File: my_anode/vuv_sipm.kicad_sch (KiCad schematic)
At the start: 8 parts

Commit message: Add files via upload
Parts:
- renumbered C1 to C23, C2 to C24, D1 to D12, R1 to R56, R2 to R57, R3 to R58, R4 to R59, R5 to R60
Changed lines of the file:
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@@
   (symbol (lib_id "Device:R_US") (at 139.7 77.47 270) (unit 1)
     (in_bom yes) (on_board yes) (fields_autoplaced)
-    (property "Reference" "R4" (id 0) (at 140.9701 80.01 0)
+    (property "Reference" "R59" (id 0) (at 140.9701 80.01 0)
       (effects (font (size 1.27 1.27)) (justify left))
     )
@@
   (symbol (lib_id "Device:C") (at 115.57 73.66 90) (unit 1)
     (in_bom yes) (on_board yes) (fields_autoplaced)
-    (property "Reference" "C1" (id 0) (at 115.57 66.04 90))
+    (property "Reference" "C23" (id 0) (at 115.57 66.04 90))
     (property "Value" "C" (id 1) (at 115.57 68.58 90))
     (property "Footprint" "Capacitor_SMD:CP_Elec_4x3" (id 2) (at 119.38 72.6948 0)
@@
   (symbol (lib_id "Device:D_Photo") (at 124.46 91.44 180) (unit 1)
     (in_bom yes) (on_board yes) (fields_autoplaced)
-    (property "Reference" "D1" (id 0) (at 125.4125 85.09 0))
+    (property "Reference" "D12" (id 0) (at 125.4125 85.09 0))
     (property "Value" "D_Photo" (id 1) (at 125.4125 87.63 0))
     (property "Footprint" "OptoDevice:S13370-6075CN" (id 2) (at 125.73 91.44 0)
@@
   (symbol (lib_id "Device:R_US") (at 104.14 77.47 0) (unit 1)
     (in_bom yes) (on_board yes) (fields_autoplaced)
-    (property "Reference" "R1" (id 0) (at 106.68 76.1999 0)
+    (property "Reference" "R56" (id 0) (at 106.68 76.1999 0)
       (effects (font (size 1.27 1.27)) (justify left))
     )
@@
   (symbol (lib_id "Device:R_US") (at 113.03 88.9 0) (unit 1)
     (in_bom yes) (on_board yes) (fields_autoplaced)
-    (property "Reference" "R2" (id 0) (at 115.57 87.6299 0)
+    (property "Reference" "R57" (id 0) (at 115.57 87.6299 0)
       (effects (font (size 1.27 1.27)) (justify left))
     )
@@
   (symbol (lib_id "Device:R_US") (at 148.59 73.66 0) (unit 1)
     (in_bom yes) (on_board yes) (fields_autoplaced)
-    (property "Reference" "R5" (id 0) (at 151.13 72.3899 0)
+    (property "Reference" "R60" (id 0) (at 151.13 72.3899 0)
       (effects (font (size 1.27 1.27)) (justify left))
     )
@@
   (symbol (lib_id "Device:C") (at 140.97 93.98 0) (unit 1)
     (in_bom yes) (on_board yes) (fields_autoplaced)
-    (property "Reference" "C2" (id 0) (at 144.78 92.7099 0)
+    (property "Reference" "C24" (id 0) (at 144.78 92.7099 0)
       (effects (font (size 1.27 1.27)) (justify left))
     )
@@
   (symbol (lib_id "Device:R_US") (at 134.62 97.79 90) (unit 1)
     (in_bom yes) (on_board yes) (fields_autoplaced)
-    (property "Reference" "R3" (id 0) (at 133.3499 95.25 0)
+    (property "Reference" "R58" (id 0) (at 133.3499 95.25 0)
       (effects (font (size 1.27 1.27)) (justify left))
     )

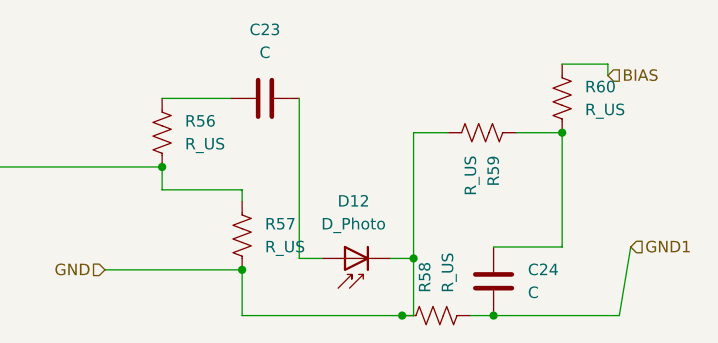
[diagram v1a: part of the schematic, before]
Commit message: Add quarter-anode board
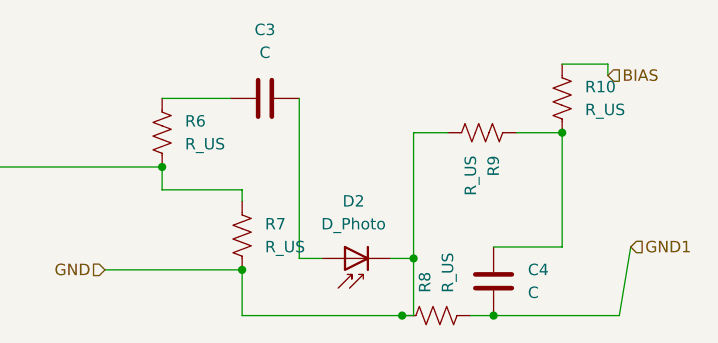
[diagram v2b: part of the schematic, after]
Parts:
- C3: renamed from C23; footprint Capacitor_SMD:CP_Elec_4x3 -> Capacitor_SMD:C_1812_4532Metric_Pad1.57x3.40mm_HandSolder
- C4: renamed from C24; footprint Capacitor_SMD:CP_Elec_4x3 -> Capacitor_SMD:C_1812_4532Metric_Pad1.57x3.40mm_HandSolder
- renumbered D12 to D2, R60 to R10, R56 to R6, R57 to R7, R58 to R8, R59 to R9
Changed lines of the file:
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@@
   (symbol (lib_id "Device:R_US") (at 139.7 77.47 270) (unit 1)
     (in_bom yes) (on_board yes) (fields_autoplaced)
-    (property "Reference" "R59" (id 0) (at 140.9701 80.01 0)
+    (property "Reference" "R9" (id 0) (at 140.9701 80.01 0)
       (effects (font (size 1.27 1.27)) (justify left))
     )
@@
   (symbol (lib_id "Device:C") (at 115.57 73.66 90) (unit 1)
     (in_bom yes) (on_board yes) (fields_autoplaced)
-    (property "Reference" "C23" (id 0) (at 115.57 66.04 90))
+    (property "Reference" "C3" (id 0) (at 115.57 66.04 90))
     (property "Value" "C" (id 1) (at 115.57 68.58 90))
-    (property "Footprint" "Capacitor_SMD:CP_Elec_4x3" (id 2) (at 119.38 72.6948 0)
+    (property "Footprint" "Capacitor_SMD:C_1812_4532Metric_Pad1.57x3.40mm_HandSolder" (id 2) (at 119.38 72.6948 0)
       (effects (font (size 1.27 1.27)) hide)
     )
@@
   (symbol (lib_id "Device:D_Photo") (at 124.46 91.44 180) (unit 1)
     (in_bom yes) (on_board yes) (fields_autoplaced)
-    (property "Reference" "D12" (id 0) (at 125.4125 85.09 0))
+    (property "Reference" "D2" (id 0) (at 125.4125 85.09 0))
     (property "Value" "D_Photo" (id 1) (at 125.4125 87.63 0))
     (property "Footprint" "OptoDevice:S13370-6075CN" (id 2) (at 125.73 91.44 0)
@@
   (symbol (lib_id "Device:R_US") (at 104.14 77.47 0) (unit 1)
     (in_bom yes) (on_board yes) (fields_autoplaced)
-    (property "Reference" "R56" (id 0) (at 106.68 76.1999 0)
+    (property "Reference" "R6" (id 0) (at 106.68 76.1999 0)
       (effects (font (size 1.27 1.27)) (justify left))
     )
@@
   (symbol (lib_id "Device:R_US") (at 113.03 88.9 0) (unit 1)
     (in_bom yes) (on_board yes) (fields_autoplaced)
-    (property "Reference" "R57" (id 0) (at 115.57 87.6299 0)
+    (property "Reference" "R7" (id 0) (at 115.57 87.6299 0)
       (effects (font (size 1.27 1.27)) (justify left))
     )
@@
   (symbol (lib_id "Device:R_US") (at 148.59 73.66 0) (unit 1)
     (in_bom yes) (on_board yes) (fields_autoplaced)
-    (property "Reference" "R60" (id 0) (at 151.13 72.3899 0)
+    (property "Reference" "R10" (id 0) (at 151.13 72.3899 0)
       (effects (font (size 1.27 1.27)) (justify left))
     )
@@
   (symbol (lib_id "Device:C") (at 140.97 93.98 0) (unit 1)
     (in_bom yes) (on_board yes) (fields_autoplaced)
-    (property "Reference" "C24" (id 0) (at 144.78 92.7099 0)
+    (property "Reference" "C4" (id 0) (at 144.78 92.7099 0)
       (effects (font (size 1.27 1.27)) (justify left))
     )
@@
       (effects (font (size 1.27 1.27)) (justify left))
     )
-    (property "Footprint" "Capacitor_SMD:CP_Elec_4x3" (id 2) (at 141.9352 97.79 0)
+    (property "Footprint" "Capacitor_SMD:C_1812_4532Metric_Pad1.57x3.40mm_HandSolder" (id 2) (at 141.9352 97.79 0)
       (effects (font (size 1.27 1.27)) hide)
     )
@@
   (symbol (lib_id "Device:R_US") (at 134.62 97.79 90) (unit 1)
     (in_bom yes) (on_board yes) (fields_autoplaced)
-    (property "Reference" "R58" (id 0) (at 133.3499 95.25 0)
+    (property "Reference" "R8" (id 0) (at 133.3499 95.25 0)
       (effects (font (size 1.27 1.27)) (justify left))
     )

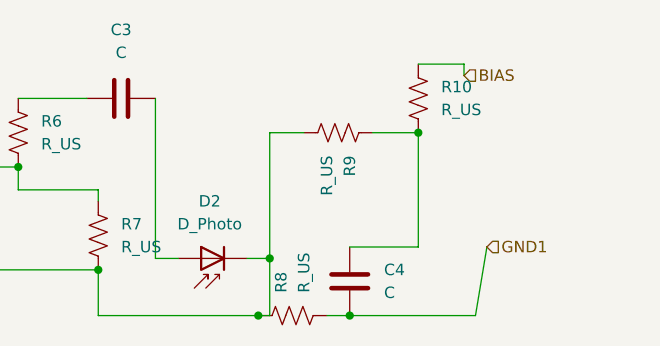
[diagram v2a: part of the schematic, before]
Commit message: Semi-final board version without voltage divider
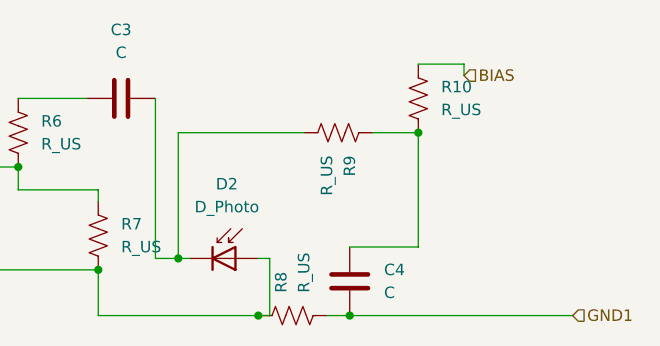
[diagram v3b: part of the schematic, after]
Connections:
- net GND: now also D2.2 (A); no longer D2.1 (K), R9.2
- net at C3.2: now also D2.1 (K), R9.2; no longer D2.2 (A)
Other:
- moved on the sheet: D2
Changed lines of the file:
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@@
   (junction (at 113.03 92.71) (diameter 0) (color 0 0 0 0)
   )
-  (junction (at 132.08 91.44) (diameter 0) (color 0 0 0 0)
+  (junction (at 121.92 91.44) (diameter 0) (color 0 0 0 0)
   )
   (junction (at 104.14 81.28) (diameter 0) (color 0 0 0 0)
@@
     (stroke (width 0) (type default) (color 0 0 0 0))
   )
-  (wire (pts (xy 154.94 97.79) (xy 156.21 90.17))
+  (wire (pts (xy 121.92 91.44) (xy 123.19 91.44))
     (stroke (width 0) (type default) (color 0 0 0 0))
   )
@@
     (stroke (width 0) (type default) (color 0 0 0 0))
   )
-  (wire (pts (xy 140.97 97.79) (xy 154.94 97.79))
+  (wire (pts (xy 140.97 97.79) (xy 165.735 97.79))
+    (stroke (width 0) (type default) (color 0 0 0 0))
+  )
+  (wire (pts (xy 121.92 77.47) (xy 121.92 91.44))
     (stroke (width 0) (type default) (color 0 0 0 0))
   )
@@
     (stroke (width 0) (type default) (color 0 0 0 0))
   )
-  (wire (pts (xy 113.03 83.82) (xy 113.03 85.09))
+  (wire (pts (xy 130.81 91.44) (xy 132.08 91.44))
     (stroke (width 0) (type default) (color 0 0 0 0))
   )
-  (wire (pts (xy 132.08 91.44) (xy 132.08 77.47))
+  (wire (pts (xy 113.03 83.82) (xy 113.03 85.09))
     (stroke (width 0) (type default) (color 0 0 0 0))
   )
@@
     (stroke (width 0) (type default) (color 0 0 0 0))
   )
-  (wire (pts (xy 129.54 91.44) (xy 132.08 91.44))
-    (stroke (width 0) (type default) (color 0 0 0 0))
-  )
   (wire (pts (xy 138.43 97.79) (xy 140.97 97.79))
     (stroke (width 0) (type default) (color 0 0 0 0))
@@
     (stroke (width 0) (type default) (color 0 0 0 0))
   )
-  (wire (pts (xy 132.08 77.47) (xy 135.89 77.47))
+  (wire (pts (xy 121.92 77.47) (xy 135.89 77.47))
     (stroke (width 0) (type default) (color 0 0 0 0))
   )
@@
     (effects (font (size 1.27 1.27)) (justify right))
   )
-  (hierarchical_label "GND1" (shape input) (at 156.21 90.17 0)
+  (hierarchical_label "GND1" (shape input) (at 165.735 97.79 0)
     (effects (font (size 1.27 1.27)) (justify left))
   )
@@
     (pin "2")
   )
-  (symbol (lib_id "Device:D_Photo") (at 124.46 91.44 180) (unit 1)
+  (symbol (lib_id "Device:D_Photo") (at 128.27 91.44 0) (unit 1)
     (in_bom yes) (on_board yes) (fields_autoplaced)
-    (property "Reference" "D2" (id 0) (at 125.4125 85.09 0))
-    (property "Value" "D_Photo" (id 1) (at 125.4125 87.63 0))
-    (property "Footprint" "OptoDevice:S13370-6075CN" (id 2) (at 125.73 91.44 0)
+    (property "Reference" "D2" (id 0) (at 127.3175 83.185 0))
+    (property "Value" "D_Photo" (id 1) (at 127.3175 85.725 0))
+    (property "Footprint" "OptoDevice:S13370-6075CN" (id 2) (at 127 91.44 0)
       (effects (font (size 1.27 1.27)) hide)
     )
-    (property "Datasheet" "~" (id 3) (at 125.73 91.44 0)
+    (property "Datasheet" "~" (id 3) (at 127 91.44 0)
       (effects (font (size 1.27 1.27)) hide)
     )

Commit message: Add files via upload
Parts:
- added R23: R_US, Resistor_SMD:R_0402_1005Metric, symbol Device:R_US
- added R24: R_Variable_US, Potentiometer_SMD:Potentiometer_Bourns_3214G_Horizontal, symbol Device:R_Variable_US
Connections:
- net BIAS: now also R24.2; no longer R10.1
- net GND1: now also R23.2
- new net: R10.1, R23.1, R24.1
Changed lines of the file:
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@@
 (kicad_sch (version 20211123) (generator eeschema)
   (paper "A4")
+  (junction (at 161.925 97.79) (diameter 0) (color 0 0 0 0)
+  )
   (junction (at 148.59 77.47) (diameter 0) (color 0 0 0 0)
   )
@@
   (junction (at 130.81 97.79) (diameter 0) (color 0 0 0 0)
   )
+  (junction (at 157.48 69.85) (diameter 0) (color 0 0 0 0)
+  )
   (junction (at 140.97 97.79) (diameter 0) (color 0 0 0 0)
   )
@@
     (stroke (width 0) (type default) (color 0 0 0 0))
   )
+  (wire (pts (xy 157.48 74.295) (xy 157.48 69.85))
+    (stroke (width 0) (type default) (color 0 0 0 0))
+  )
   (wire (pts (xy 132.08 91.44) (xy 132.08 97.79))
     (stroke (width 0) (type default) (color 0 0 0 0))
   )
+  (wire (pts (xy 167.64 69.85) (xy 176.53 69.85))
+    (stroke (width 0) (type default) (color 0 0 0 0))
+  )
   (wire (pts (xy 121.92 91.44) (xy 123.19 91.44))
     (stroke (width 0) (type default) (color 0 0 0 0))
   )
-  (wire (pts (xy 153.67 69.85) (xy 153.67 71.12))
-    (stroke (width 0) (type default) (color 0 0 0 0))
-  )
-  (wire (pts (xy 140.97 97.79) (xy 165.735 97.79))
+  (wire (pts (xy 140.97 97.79) (xy 161.925 97.79))
     (stroke (width 0) (type default) (color 0 0 0 0))
   )
@@
     (stroke (width 0) (type default) (color 0 0 0 0))
   )
+  (wire (pts (xy 157.48 69.85) (xy 160.02 69.85))
+    (stroke (width 0) (type default) (color 0 0 0 0))
+  )
   (wire (pts (xy 130.81 97.79) (xy 132.08 97.79))
     (stroke (width 0) (type default) (color 0 0 0 0))
@@
     (stroke (width 0) (type default) (color 0 0 0 0))
   )
+  (wire (pts (xy 161.925 81.28) (xy 161.925 74.295))
+    (stroke (width 0) (type default) (color 0 0 0 0))
+  )
+  (wire (pts (xy 161.925 88.9) (xy 161.925 97.79))
+    (stroke (width 0) (type default) (color 0 0 0 0))
+  )
+  (wire (pts (xy 161.925 74.295) (xy 157.48 74.295))
+    (stroke (width 0) (type default) (color 0 0 0 0))
+  )
   (wire (pts (xy 104.14 81.28) (xy 104.14 83.82))
     (stroke (width 0) (type default) (color 0 0 0 0))
   )
+  (wire (pts (xy 148.59 69.85) (xy 157.48 69.85))
+    (stroke (width 0) (type default) (color 0 0 0 0))
+  )
   (wire (pts (xy 140.97 90.17) (xy 148.59 90.17))
     (stroke (width 0) (type default) (color 0 0 0 0))
@@
     (stroke (width 0) (type default) (color 0 0 0 0))
   )
+  (wire (pts (xy 161.925 97.79) (xy 165.735 97.79))
+    (stroke (width 0) (type default) (color 0 0 0 0))
+  )
   (wire (pts (xy 138.43 97.79) (xy 140.97 97.79))
     (stroke (width 0) (type default) (color 0 0 0 0))
@@
   )
   (wire (pts (xy 119.38 91.44) (xy 121.92 91.44))
-    (stroke (width 0) (type default) (color 0 0 0 0))
-  )
-  (wire (pts (xy 148.59 69.85) (xy 153.67 69.85))
     (stroke (width 0) (type default) (color 0 0 0 0))
   )
@@
     (effects (font (size 1.27 1.27)) (justify right))
   )
-  (hierarchical_label "BIAS" (shape input) (at 153.67 71.12 0)
+  (hierarchical_label "BIAS" (shape input) (at 176.53 69.85 0)
     (effects (font (size 1.27 1.27)) (justify left))
   )
@@
     (pin "2")
   )
+  (symbol (lib_id "Device:R_Variable_US") (at 163.83 69.85 90) (unit 1)
+    (in_bom yes) (on_board yes) (fields_autoplaced)
+    (property "Reference" "R24" (id 0) (at 163.7919 62.23 90))
+    (property "Value" "R_Variable_US" (id 1) (at 163.7919 64.77 90))
+    (property "Footprint" "Potentiometer_SMD:Potentiometer_Bourns_3214G_Horizontal" (id 2) (at 163.83 71.628 90)
+      (effects (font (size 1.27 1.27)) hide)
+    )
+    (property "Datasheet" "~" (id 3) (at 163.83 69.85 0)
+      (effects (font (size 1.27 1.27)) hide)
+    )
+    (pin "1")
+    (pin "2")
+  )
   (symbol (lib_id "Device:R_US") (at 113.03 88.9 0) (unit 1)
     (in_bom yes) (on_board yes) (fields_autoplaced)
@@
       (effects (font (size 1.27 1.27)) hide)
     )
+    (pin "1")
+    (pin "2")
+  )
+  (symbol (lib_id "Device:R_US") (at 161.925 85.09 0) (unit 1)
+    (in_bom yes) (on_board yes) (fields_autoplaced)
+    (property "Reference" "R23" (id 0) (at 163.83 83.8199 0)
+      (effects (font (size 1.27 1.27)) (justify left))
+    )
+    (property "Value" "R_US" (id 1) (at 163.83 86.3599 0)
+      (effects (font (size 1.27 1.27)) (justify left))
+    )
+    (property "Footprint" "Resistor_SMD:R_0402_1005Metric" (id 2) (at 162.941 85.344 90)
+      (effects (font (size 1.27 1.27)) hide)
+    )
+    (property "Datasheet" "~" (id 3) (at 161.925 85.09 0)
+      (effects (font (size 1.27 1.27)) hide)
+    )

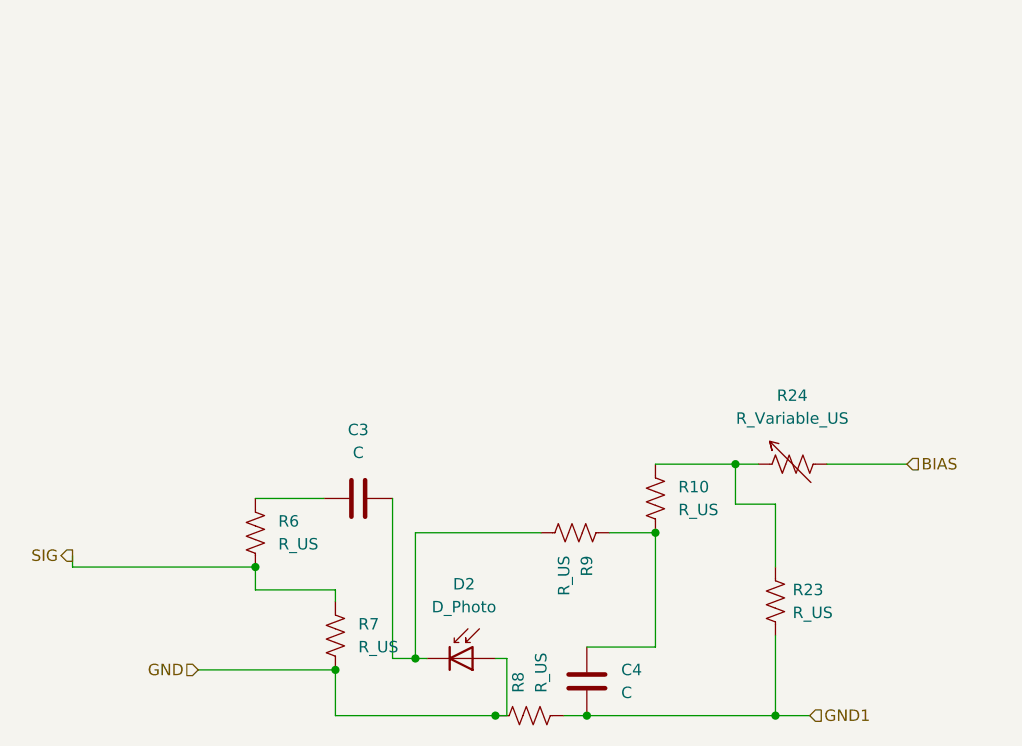
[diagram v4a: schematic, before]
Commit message: Add anode prior to copying
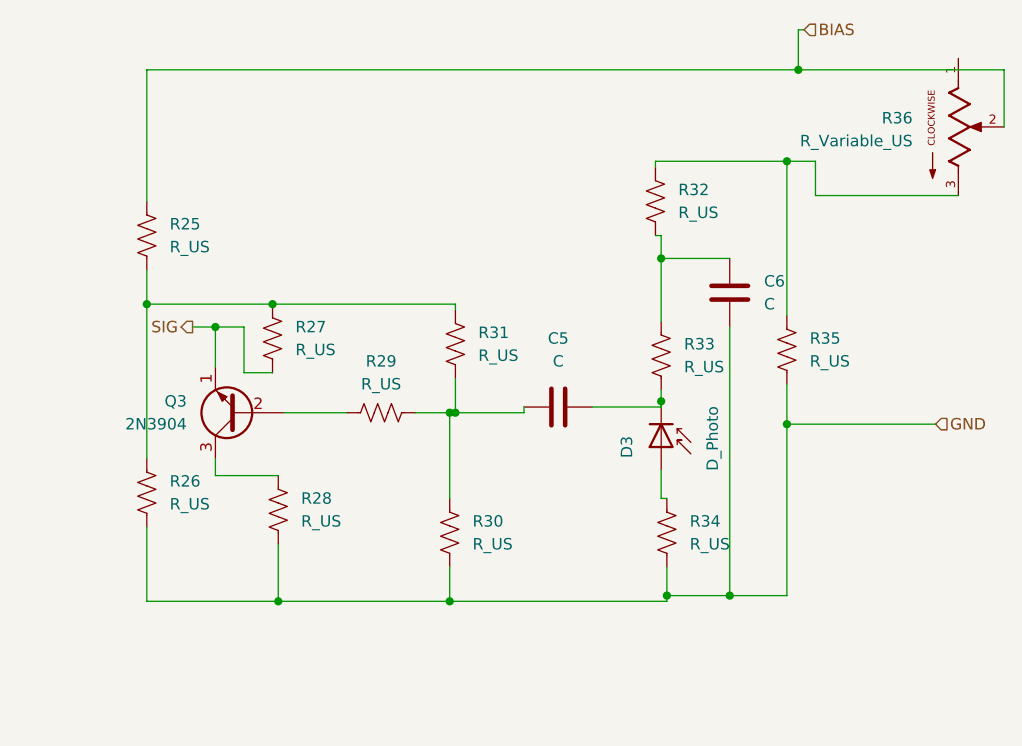
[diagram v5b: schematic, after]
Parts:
- removed R10, R23, R6, R7, R8, R9: R_US, Resistor_SMD:R_0402_1005Metric, symbol Device:R_US
- added Q3: 2N3904, BC846BLT3G:BC846BLT3G, symbol Transistor_BJT:2N3904
- added R25, R26, R27, R28, R29, R30, R31, R32, R33, R34, R35: R_US, Resistor_SMD:R_0603_1608Metric, symbol Device:R_US
- C5: renamed from C3; footprint Capacitor_SMD:C_1812_4532Metric_Pad1.57x3.40mm_HandSolder -> Capacitor_SMD:C_1206_3216Metric
- C6: renamed from C4; footprint Capacitor_SMD:C_1812_4532Metric_Pad1.57x3.40mm_HandSolder -> Capacitor_SMD:C_1206_3216Metric
- R36: renamed from R24; footprint Potentiometer_SMD:Potentiometer_Bourns_3214G_Horizontal -> 3361P-1-104GLF:TRIM_3361P-1-104GLF; symbol Device:R_Variable_US -> 3361P-1-104GLF:3361P-1-104GLF; MANUFACTURER (none) -> Bourns; MAXIMUM_PACKAGE_HEIGHT (none) -> 5.84mm; PARTREV (none) -> 08/19; STANDARD (none) -> Manufacturer Recommendations
- renumbered D2 to D3
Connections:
- net GND1 is gone; now on net GND: C6.2
- net BIAS: now also R25.1
- net GND: now also R26.2, R28.2, R30.2, R34.2, R35.2; no longer D3.2 (A)
- net SIG: now also Q3.1 (E), R27.2
- net at C6.1: now also R32.2, R33.1
- net at C5.2, D3.1 (K): now also R33.2
- net at C5.1: now also R29.2, R30.1, R31.2
- new net: R32.1, R35.1, R36.3
- new net: D3.2 (A), R34.1
- new net: Q3.3 (C), R28.1
- new net: R25.2, R26.1, R27.1, R31.1
- new net: Q3.2 (B), R29.1
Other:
- moved on the sheet: C5, C6, D3
